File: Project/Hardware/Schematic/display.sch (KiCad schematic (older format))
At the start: 4 parts

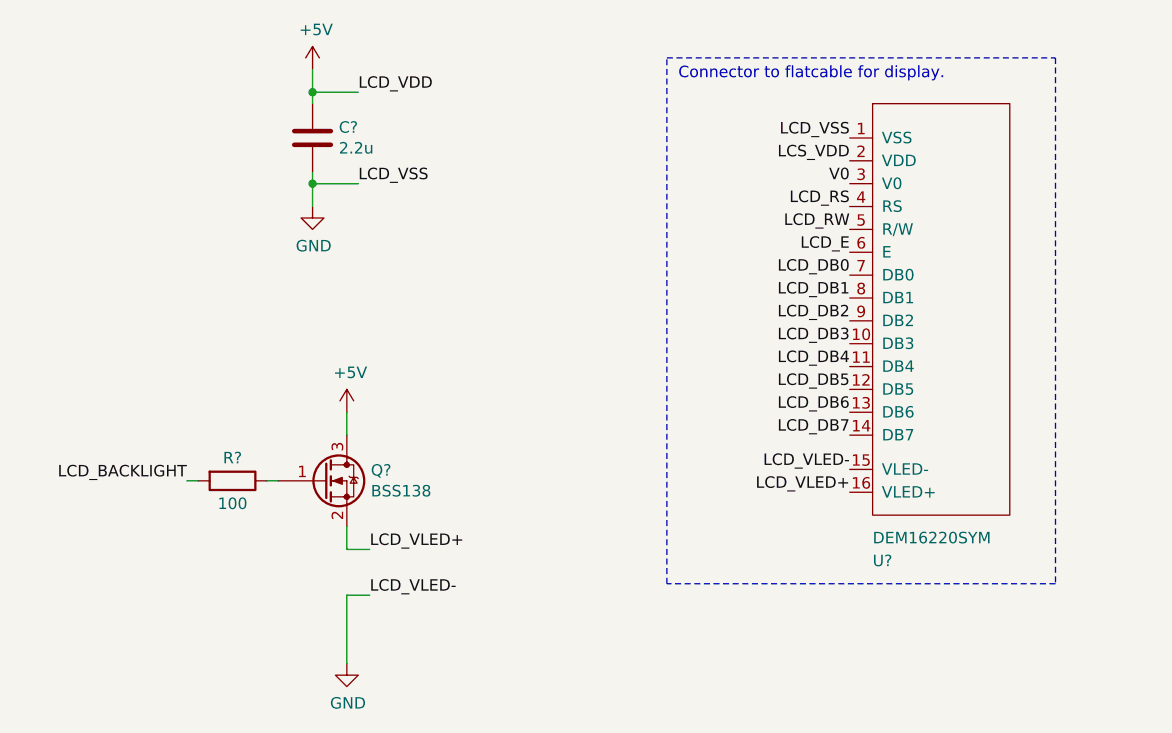
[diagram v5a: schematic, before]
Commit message: Pulse, piezo och labels (#8)
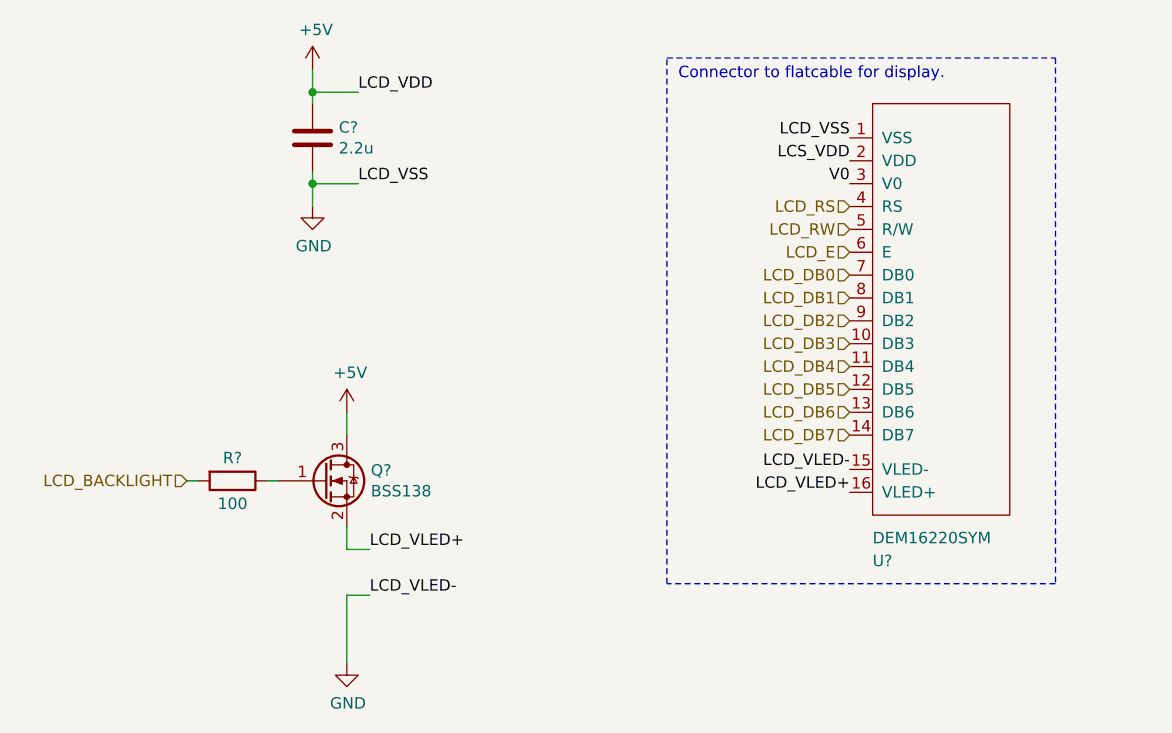
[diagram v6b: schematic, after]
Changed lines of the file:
@@
 	1    0    0    -1
 $EndComp
-Text Label 1200 2750 2    50   ~ 0
-LCD_BACKLIGHT
 Wire Wire Line
 	1900 2550 1900 2450
@@
 Text Label 4100 1350 2    50   ~ 0
 LCS_VDD
-Text Label 4100 1550 2    50   ~ 0
-LCD_RS
-Text Label 4100 1650 2    50   ~ 0
-LCD_RW
-Text Label 4100 1750 2    50   ~ 0
-LCD_E
-Text Label 4100 1850 2    50   ~ 0
-LCD_DB0
-Text Label 4100 1950 2    50   ~ 0
-LCD_DB1
-Text Label 4100 2050 2    50   ~ 0
-LCD_DB2
-Text Label 4100 2150 2    50   ~ 0
-LCD_DB3
-Text Label 4100 2250 2    50   ~ 0
-LCD_DB4
-Text Label 4100 2350 2    50   ~ 0
-LCD_DB5
-Text Label 4100 2450 2    50   ~ 0
-LCD_DB6
-Text Label 4100 2550 2    50   ~ 0
-LCD_DB7
 Text Label 4100 2800 2    50   ~ 0
 LCD_VLED+
@@
 Wire Notes Line
 	3300 3200 3300 900
+Text HLabel 1200 2750 0    50   Input ~ 0
+LCD_BACKLIGHT
+Text HLabel 4100 1550 0    50   Input ~ 0
+LCD_RS
+Text HLabel 4100 1650 0    50   Input ~ 0
+LCD_RW
+Text HLabel 4100 1750 0    50   Input ~ 0
+LCD_E
+Text HLabel 4100 1850 0    50   Input ~ 0
+LCD_DB0
+Text HLabel 4100 1950 0    50   Input ~ 0
+LCD_DB1
+Text HLabel 4100 2050 0    50   Input ~ 0
+LCD_DB2
+Text HLabel 4100 2150 0    50   Input ~ 0
+LCD_DB3
+Text HLabel 4100 2250 0    50   Input ~ 0
+LCD_DB4
+Text HLabel 4100 2350 0    50   Input ~ 0
+LCD_DB5
+Text HLabel 4100 2450 0    50   Input ~ 0
+LCD_DB6
+Text HLabel 4100 2550 0    50   Input ~ 0
+LCD_DB7
 $EndSCHEMATC
